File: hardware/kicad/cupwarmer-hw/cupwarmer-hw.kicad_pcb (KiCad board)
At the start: 4 copper layers, 56 x 56 mm, 47 parts, among them J1 I2C Service, J3 STATUS_MON, Q1 AO3400 SOT-23, U1 STWLC38JRM

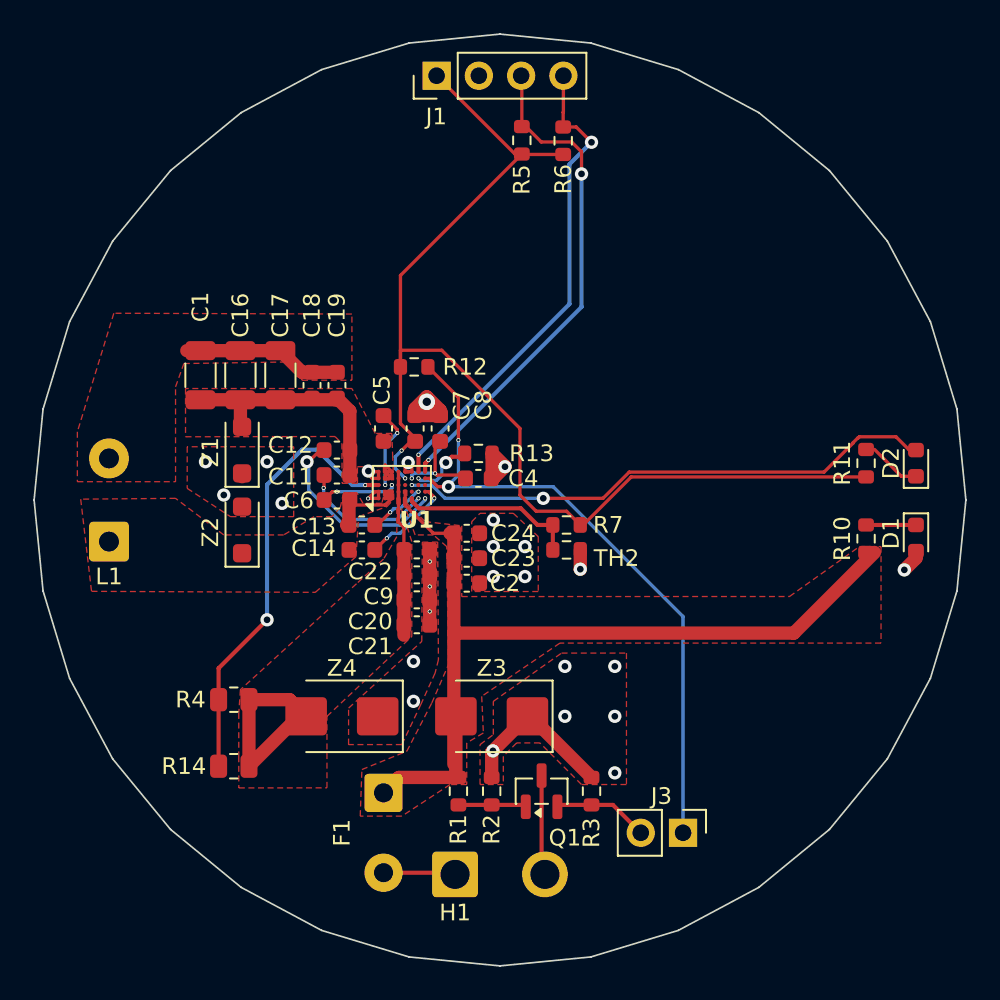
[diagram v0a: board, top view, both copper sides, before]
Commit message: Tag HEATER_IN/OUT as POWER and refresh DRC exclusions
Add HEATER_IN/HEATER_OUT labels in heater-control and assign them to
the POWER netclass. Refresh hole_to_hole DRC exclusions after the
recent PCB rework.

Co-Authored-By: Claude Opus 4.7 (1M context) <noreply@anthropic.com>
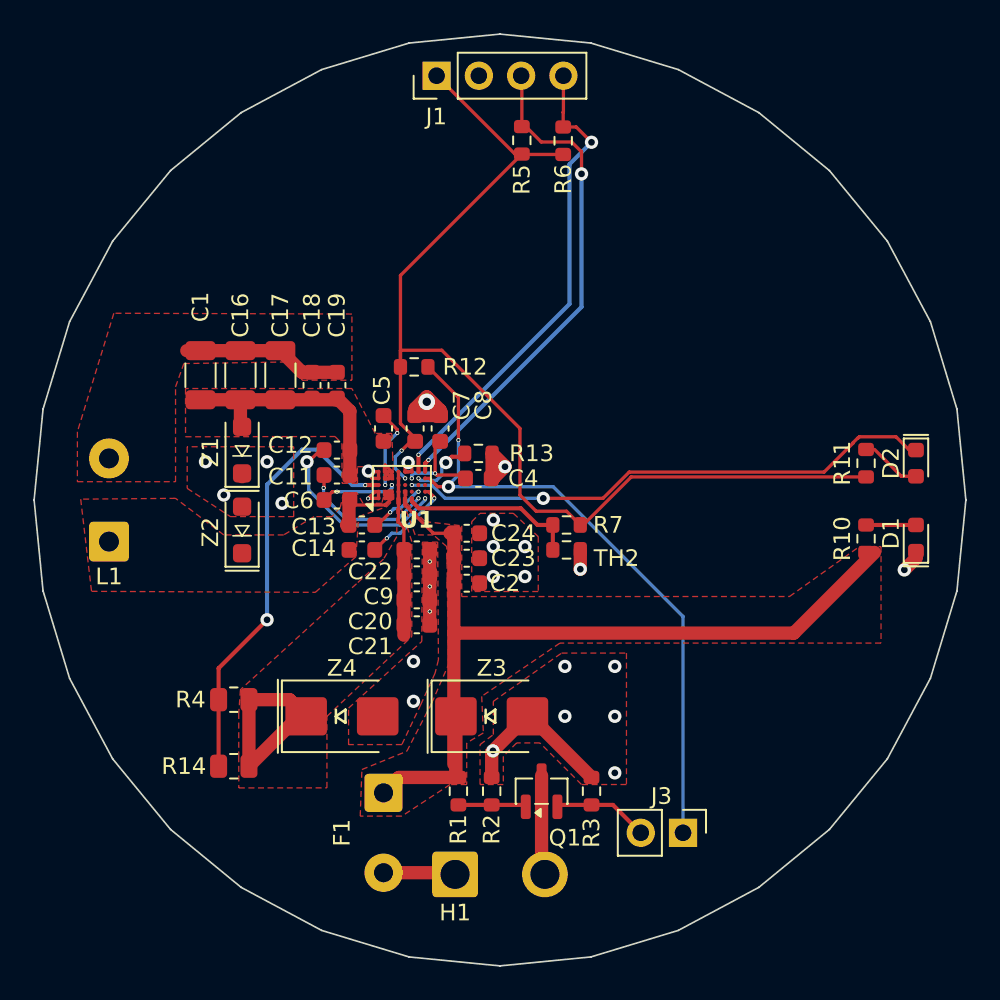
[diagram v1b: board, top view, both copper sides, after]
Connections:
- net Net-(F1-Pad2) renamed /heater-control/HEATER_IN
- net Net-(Q1-D) renamed /heater-control/HEATER_OUT

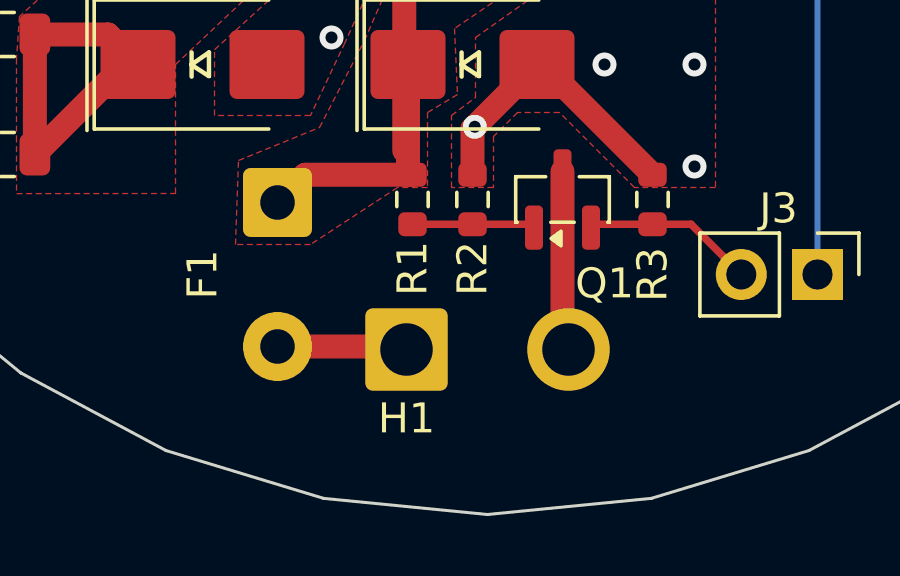
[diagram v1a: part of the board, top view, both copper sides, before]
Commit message: Add U1 BGA via-to-via DRC rule and clear hole-to-hole exclusions
Add a JLCPCB-style 0.25mm hole-to-hole rule scoped to U1 courtyard so
the BGA escape via cluster passes DRC, drop the now-unneeded
hole_to_hole exclusions, and tag I_HEATER_MON as POWER.

Co-Authored-By: Claude Opus 4.7 (1M context) <noreply@anthropic.com>
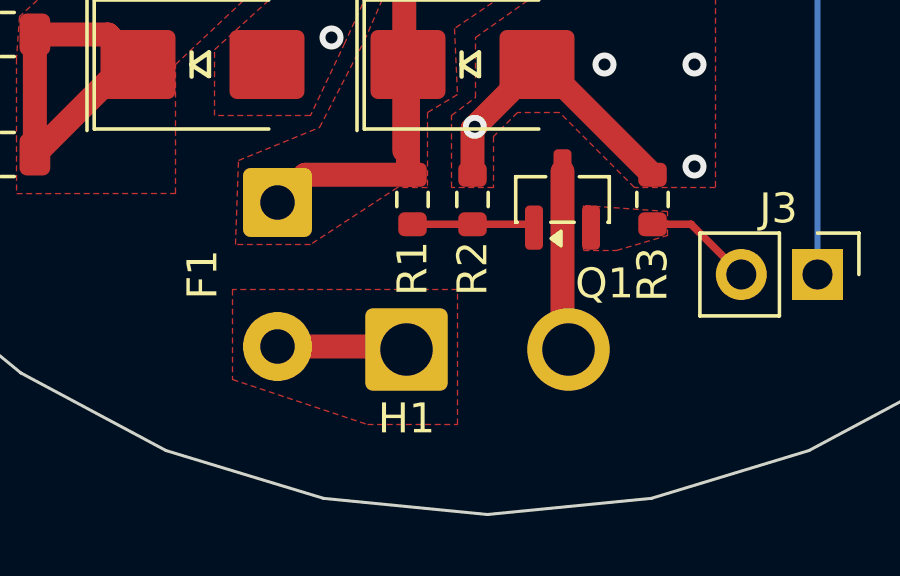
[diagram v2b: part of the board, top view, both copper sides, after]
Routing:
- net I_HEATER_MON: track 6.09 -> 3.99 mm
- added copper zone on F.Cu, net /heater-control/HEATER_IN
- added copper zone on F.Cu, net I_HEATER_MON
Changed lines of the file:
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@@
-	)
-	(segment
-		(start 105.5 118.325)
-		(end 103.5625 118.325)
-		(width 0.25)
-		(layer "F.Cu")
-		(net "I_HEATER_MON")
 	)
 	(segment
@@
 		(start 105.5 118.325)
 		(end 106.785 118.325)
-		(width 0.25)
-		(layer "F.Cu")
-		(net "I_HEATER_MON")
-	)
-	(segment
-		(start 103.5625 118.325)
-		(end 103.45 118.4375)
 		(width 0.25)
 		(layer "F.Cu")
@@
 	)
 	(zone
+		(net "I_HEATER_MON")
+		(layer "F.Cu")
+		(name "I_HEATER_MON")
+		(hatch edge 0.5)
+		(priority 12)
+		(connect_pads yes
+			(clearance 0.5)
+		)
+		(min_thickness 0.25)
+		(fill yes
+			(thermal_gap 0.5)
+			(thermal_bridge_width 0.5)
+			(island_removal_mode 0)
+		)
+		(polygon
+			(pts
+				(xy 103.2 119.2) (xy 104.3 119.2) (xy 106 118.7) (xy 106 117.9) (xy 103.2 117.7)
+			)
+		)
+	)
+	(zone
 		(net "SYS_GND")
 		(layer "F.Cu")
@@
 			)
 		)
+	)
+	(zone
+		(net "/heater-control/HEATER_IN")
+		(layer "F.Cu")
+		(name "HEATER_IN")
+		(hatch edge 0.5)
+		(priority 11)
+		(connect_pads yes
+			(clearance 0.5)
+		)
+		(min_thickness 0.25)
+		(fill yes
+			(thermal_gap 0.5)
+			(thermal_bridge_width 0.5)
+			(island_removal_mode 0)
+		)
+		(polygon
+			(pts
+				(xy 91.5 123.5) (xy 96 125) (xy 99 125) (xy 99 120.5) (xy 91.5 120.5)
+			)
+		)

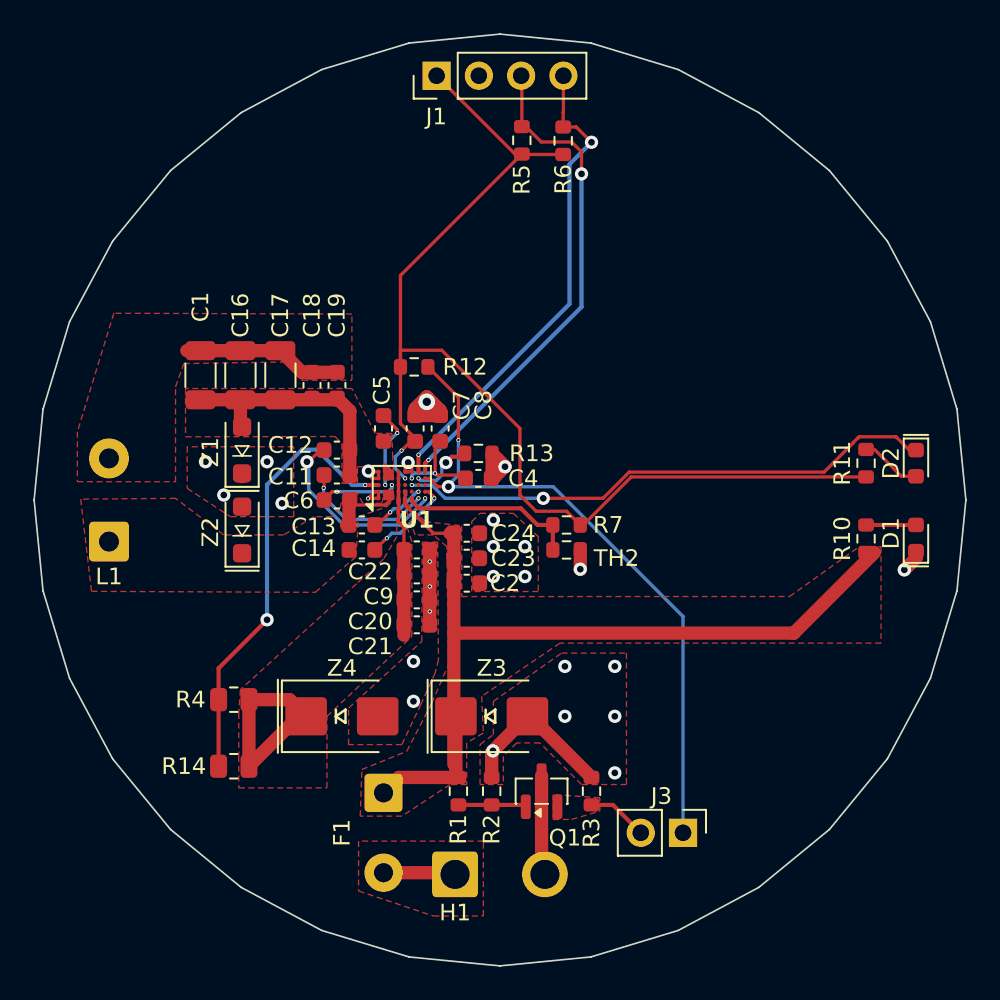
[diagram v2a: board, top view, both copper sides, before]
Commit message: Add H2/H3/H4 M2 mounting holes and nudge nearby segments
Co-Authored-By: Claude Opus 4.7 (1M context) <noreply@anthropic.com>
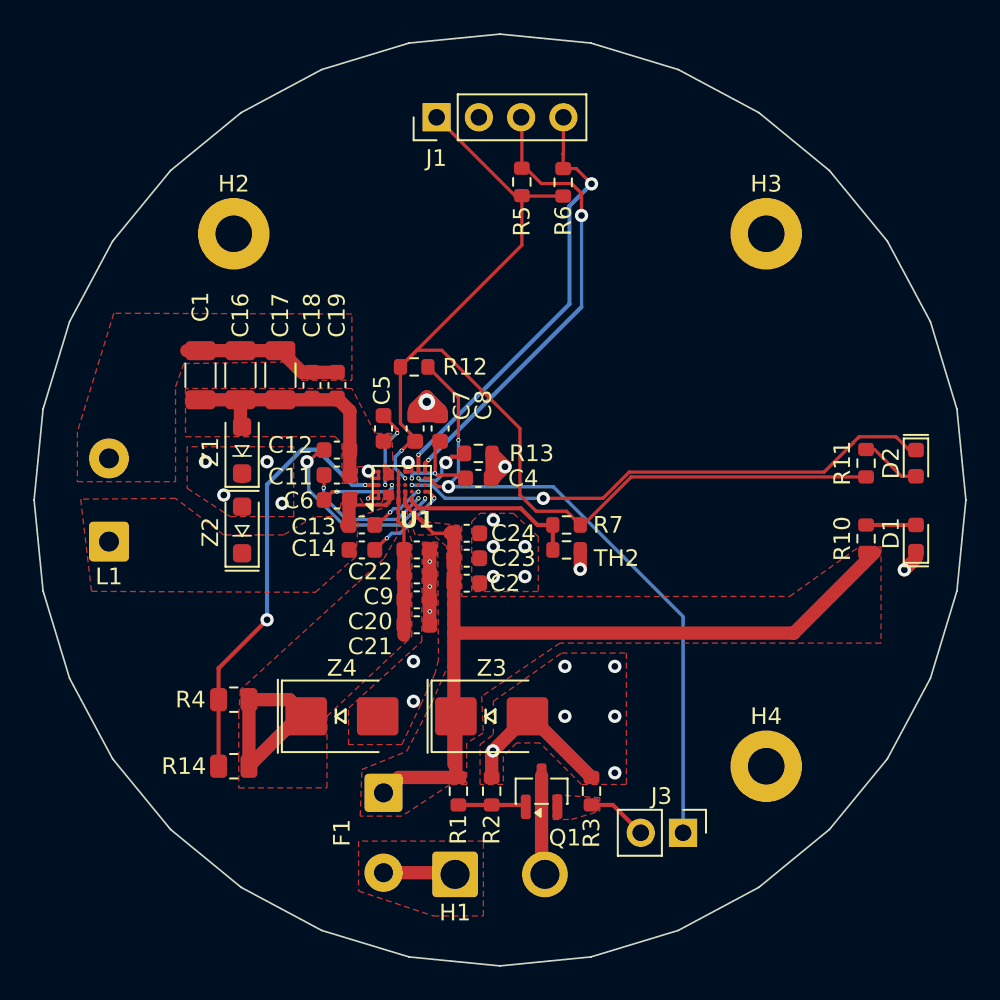
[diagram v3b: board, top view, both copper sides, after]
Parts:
- added H2: MountingHole_M2, MountingHole:MountingHole_2.2mm_M2, F.Cu at (84.0, 84.0)
- added H3: MountingHole_M2, MountingHole:MountingHole_2.2mm_M2, F.Cu at (116.0, 84.0)
- added H4: MountingHole_M2, MountingHole:MountingHole_2.2mm_M2, F.Cu at (116.0, 116.0)
- moved J1 2.50 mm to (96.2, 77.0)
- moved R5 2.50 mm to (101.3, 80.9)
- moved R6 2.50 mm to (103.8, 80.9)
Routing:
- net RX_VAA: track 70.2 -> 67.1 mm
- net I2C_SDA: track 29.3 -> 26.8 mm
- net I2C_SCL: track 30.4 -> 27.9 mm

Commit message: Add NPTH keepouts and align mounting holes to library
Add three circular rule_area keepouts (r=2.5mm, all Cu layers) under
the H2/H3/H4 M2 mounting holes so SYS_GND backs off from the screw
heads/standoffs. Rewrite H2/H3/H4 footprint bodies to match the
KiCad MountingHole_2.2mm_M2 library (correct descr/tags, version
and generator, KiLib_Generator property, Cmts.User and F.CrtYd
outline circles, F.Fab reference text, library reference/value
offsets, no extra Datasheet/Description blocks). Pads remain
2.2mm/2.2mm NPTH; copper clearance is now provided by the
keepouts. DRC clean (0 violations).

Co-Authored-By: Claude Opus 4.7 (1M context) <noreply@anthropic.com>
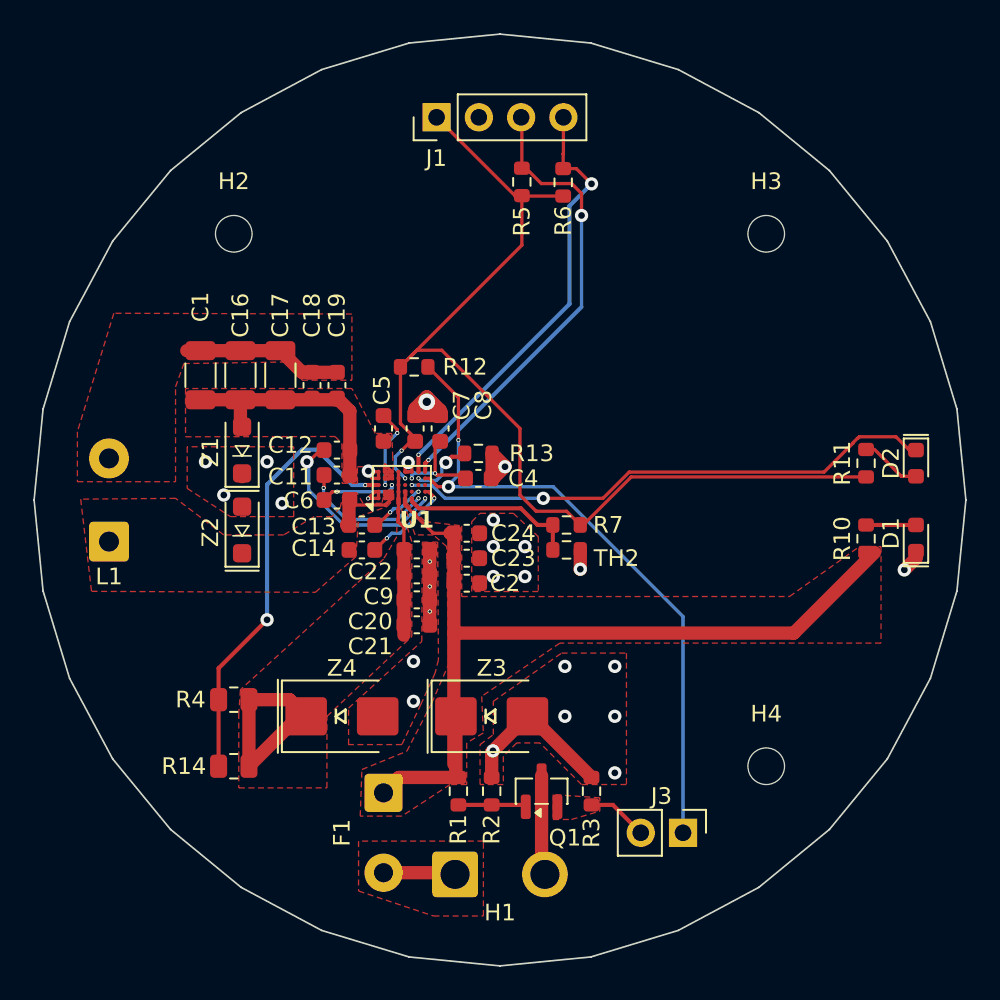
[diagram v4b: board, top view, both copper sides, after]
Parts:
- H2, H3, H4: value MountingHole_M2 -> MountingHole_2.2mm_M2
